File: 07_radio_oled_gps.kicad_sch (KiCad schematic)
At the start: 26 parts, among them J40 Amphenol MDT420E01001 E-key W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, J41 OLED A cable: GND/3V3/SCL/SDA, J45 OLED B cable: GND/3V3/SCL/SDA, U170 SN74LVC3G34DCUR E-key control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, U45 TCA9548A service I2C mux @0x70

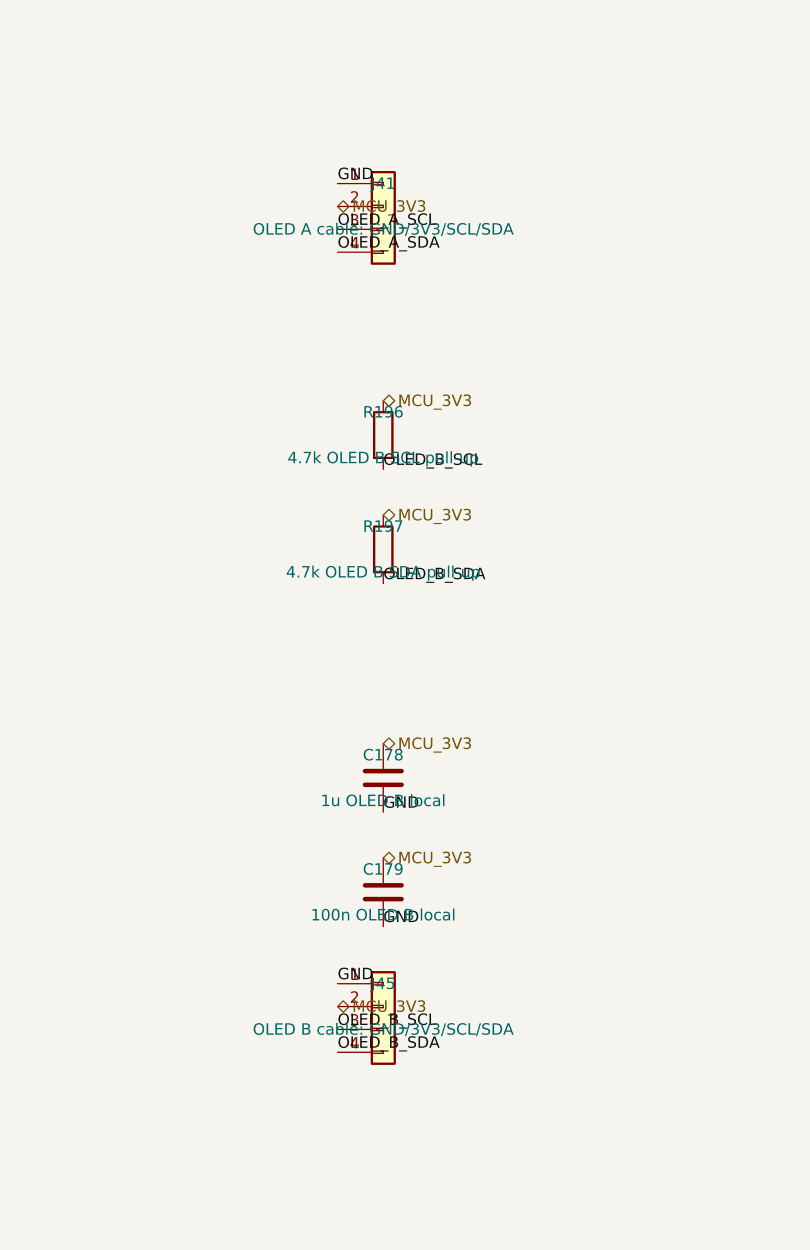
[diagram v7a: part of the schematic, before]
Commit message: get the main boards ready for routing
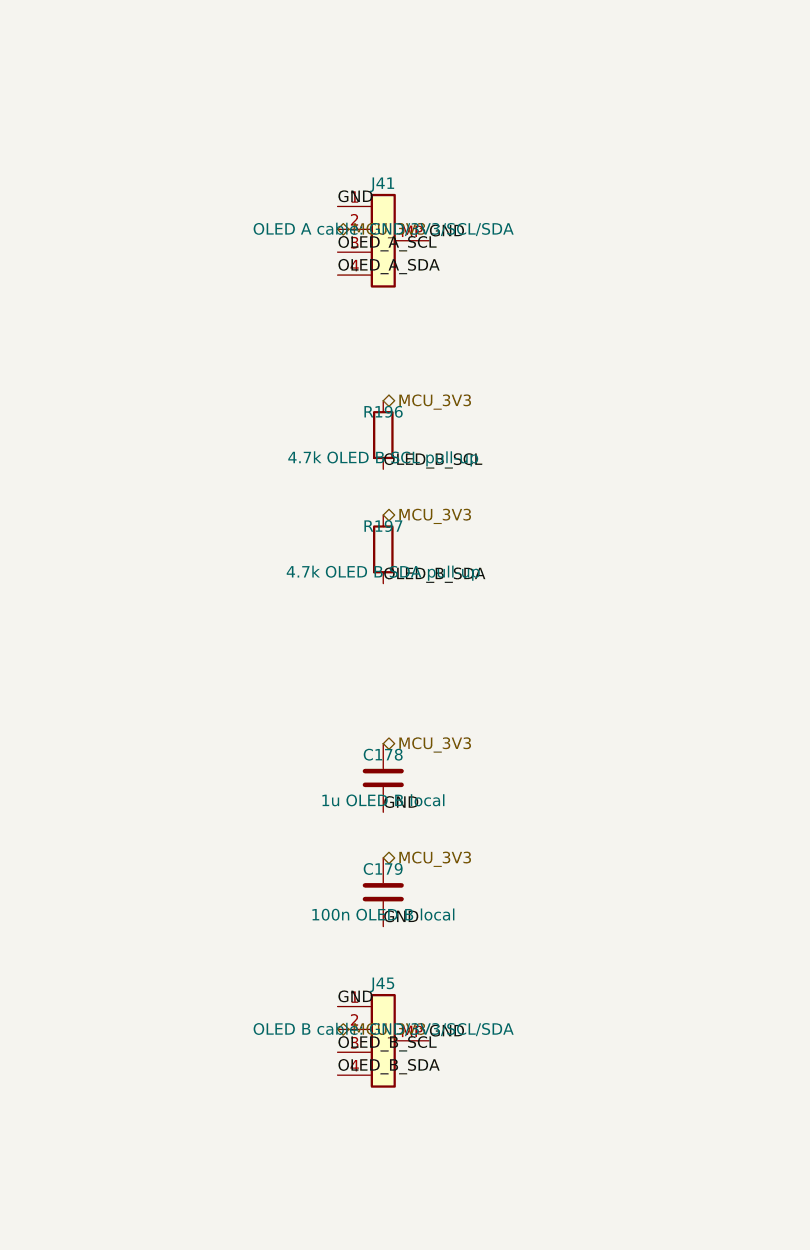
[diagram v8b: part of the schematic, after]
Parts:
- removed J45: OLED B cable: GND/3V3/SCL/SDA, Connector_JST:JST_GH_SM04B-GHS-TB_1x04-1MP_P1.25mm_Horizontal, symbol Connector_Generic:Conn_01x04
- added J45: OLED B cable: GND/3V3/SCL/SDA, Connector_JST:JST_GH_SM04B-GHS-TB_1x04-1MP_P1.25mm_Horizontal, symbol Conn_01x04_MP:Conn_01x04_MP
- J41: symbol Connector_Generic:Conn_01x04 -> Conn_01x04_MP:Conn_01x04_MP
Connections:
- net GND: now also J41.MP, J45.1 (Pin_1), J45.MP
- net MCU_3V3: now also J45.2 (Pin_2)
- net OLED_B_SCL: now also J45.3 (Pin_3)
- net OLED_B_SDA: now also J45.4 (Pin_4)
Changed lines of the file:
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@@
 )
 (symbol
-  (lib_id "Connector_Generic:Conn_01x04")
+  (lib_id "Conn_01x04_MP:Conn_01x04_MP")
   (at 204.47 287.02 0)
   (unit 1)
@@
   (pin "3")
   (pin "4")
+  (pin "MP")
   (instances
     (project "ducktop2"
@@
 )
 (label "GND"
-  (at 199.39 284.48 0)
-  (effects (font (size 1.27 1.27)) (justify left bottom))
-)
-(hierarchical_label "MCU_3V3"
-  (shape bidirectional)
   (at 199.39 287.02 0)
   (effects (font (size 1.27 1.27)) (justify left bottom))
 )
+(hierarchical_label "MCU_3V3"
+  (shape bidirectional)
+  (at 199.39 289.56 0)
+  (effects (font (size 1.27 1.27)) (justify left bottom))
+)
 (label "OLED_A_SCL"
-  (at 199.39 289.56 0)
+  (at 199.39 292.1 0)
   (effects (font (size 1.27 1.27)) (justify left bottom))
 )
 (label "OLED_A_SDA"
-  (at 199.39 292.1 0)
+  (at 199.39 294.64 0)
+  (effects (font (size 1.27 1.27)) (justify left bottom))
+)
+(label "GND"
+  (at 209.55 290.83 0)
   (effects (font (size 1.27 1.27)) (justify left bottom))
 )
@@
 )
 (symbol
-  (lib_id "Connector_Generic:Conn_01x04")
+  (lib_id "Conn_01x04_MP:Conn_01x04_MP")
   (at 204.47 375.92 0)
   (unit 1)
@@
   (pin "3")
   (pin "4")
+  (pin "MP")
   (instances
     (project "ducktop2"
@@
 )
 (label "GND"
-  (at 199.39 373.38 0)
-  (effects (font (size 1.27 1.27)) (justify left bottom))
-)
-(hierarchical_label "MCU_3V3"
-  (shape bidirectional)
   (at 199.39 375.92 0)
   (effects (font (size 1.27 1.27)) (justify left bottom))
 )
+(hierarchical_label "MCU_3V3"
+  (shape bidirectional)
+  (at 199.39 378.46 0)
+  (effects (font (size 1.27 1.27)) (justify left bottom))
+)
 (label "OLED_B_SCL"
-  (at 199.39 378.46 0)
+  (at 199.39 381 0)
   (effects (font (size 1.27 1.27)) (justify left bottom))
 )
 (label "OLED_B_SDA"
-  (at 199.39 381 0)
-  (effects (font (size 1.27 1.27)) (justify left bottom))
-)
+  (at 199.39 383.54 0)
+  (effects (font (size 1.27 1.27)) (justify left bottom))
+)
+(label "GND"
+  (at 209.55 379.73 0)
+  (effects (font (size 1.27 1.27)) (justify left bottom))
+)
